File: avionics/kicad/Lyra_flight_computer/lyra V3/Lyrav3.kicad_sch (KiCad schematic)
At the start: 84 parts, among them J2 Screw_Terminal_01x06, J3 Conn_01x02, J4 Conn_01x02, J5 Conn_01x03, J6 Conn_01x06, J7 USB_B_Micro, J8 Conn_01x04, J9 Screw_Terminal_01x06, Q1 AO3401A, Q2 AO3400A, Q3 AO3400A, Q4 AO3400A, Q5 AO3400A, U1 AZ1117-3.3, U2 BMI088, U3 MPL3115A2, U4 ADXL375BCCZ-RL7, U5 LIS3MDL, U6 ADS1015IDGS, U7 W25Q64JVXGIQ, U8 RP2040, X1 S3D12.288000B20F30T

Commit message: real pretrip
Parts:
- removed C28: 100n, Capacitor_SMD:C_0603_1608Metric, symbol Device:C_Small
- removed R22: 1k, Resistor_SMD:R_0603_1608Metric, symbol Device:R_Small
- removed U7: W25Q64JVXGIQ, Package_SO:SOIC-8_5.23x5.23mm_P1.27mm, symbol easyeda2kicad:W25Q64JVXGIQ
- added C27: 100n, Capacitor_SMD:C_0603_1608Metric, symbol Device:C_Small
- added R14: 1k, Resistor_SMD:R_0603_1608Metric, symbol Device:R_Small
- added U9: W25Q128JVS, Package_SO:SOIC-8_5.23x5.23mm_P1.27mm, symbol Memory_Flash:W25Q128JVS
- J5: LCSC Part C160403 -> (none)
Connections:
- net +3V3: now also C27.1, U9.8 (VCC)
- net BOOTSEL: now also R14.2
- net GND: now also C27.2, U9.4 (GND)
- net QSPI_SCLK: now also U9.6 (CLK)
- net QSPI_SD1: now also U9.2 (DO(IO1))
- net QSPI_SD2: now also U9.3 (IO2)
- net QSPI_SD3: now also U9.7 (IO3)
- net QSPI_SDO: now also U9.5 (DI(IO0))
- net QSPI_SS: now also R14.1, U9.1 (~{CS})
- no-connect marks 30 -> 29

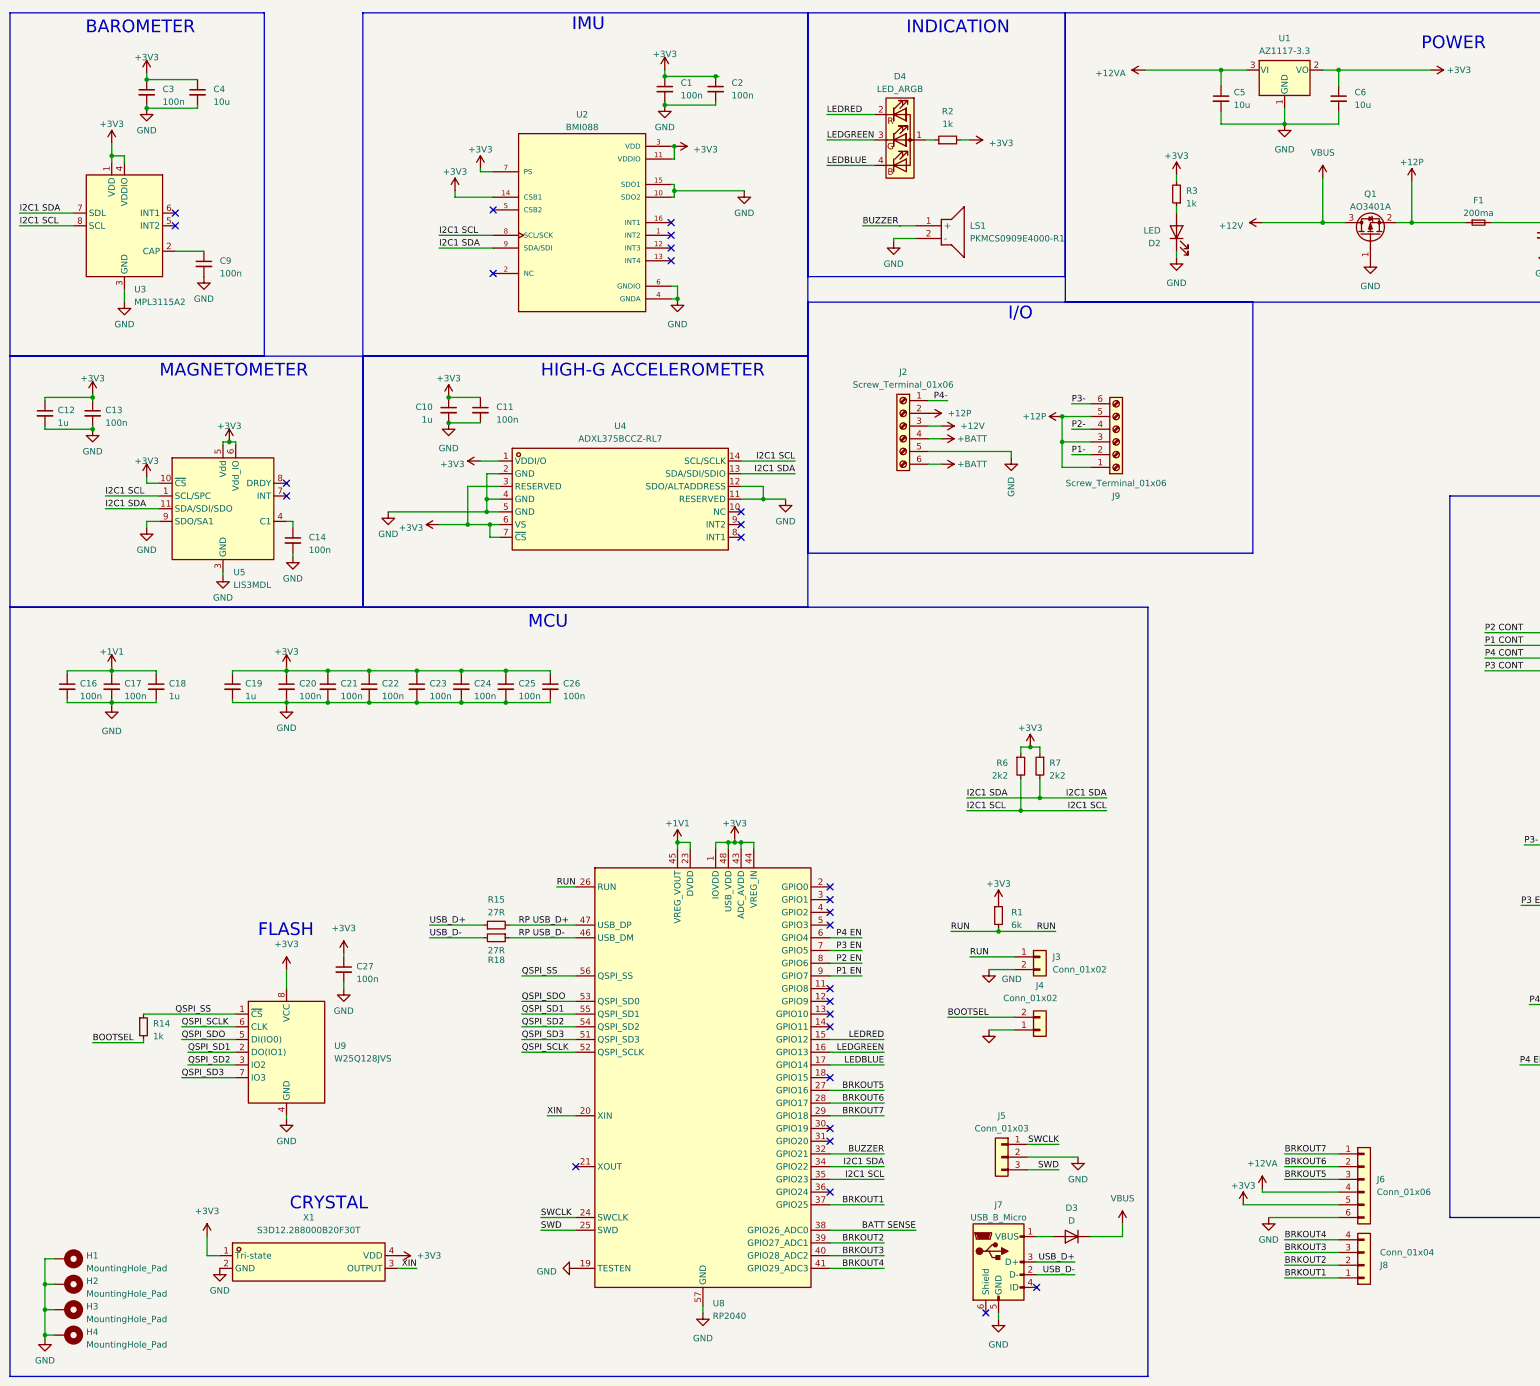
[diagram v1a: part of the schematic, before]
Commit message: change baro to dps310
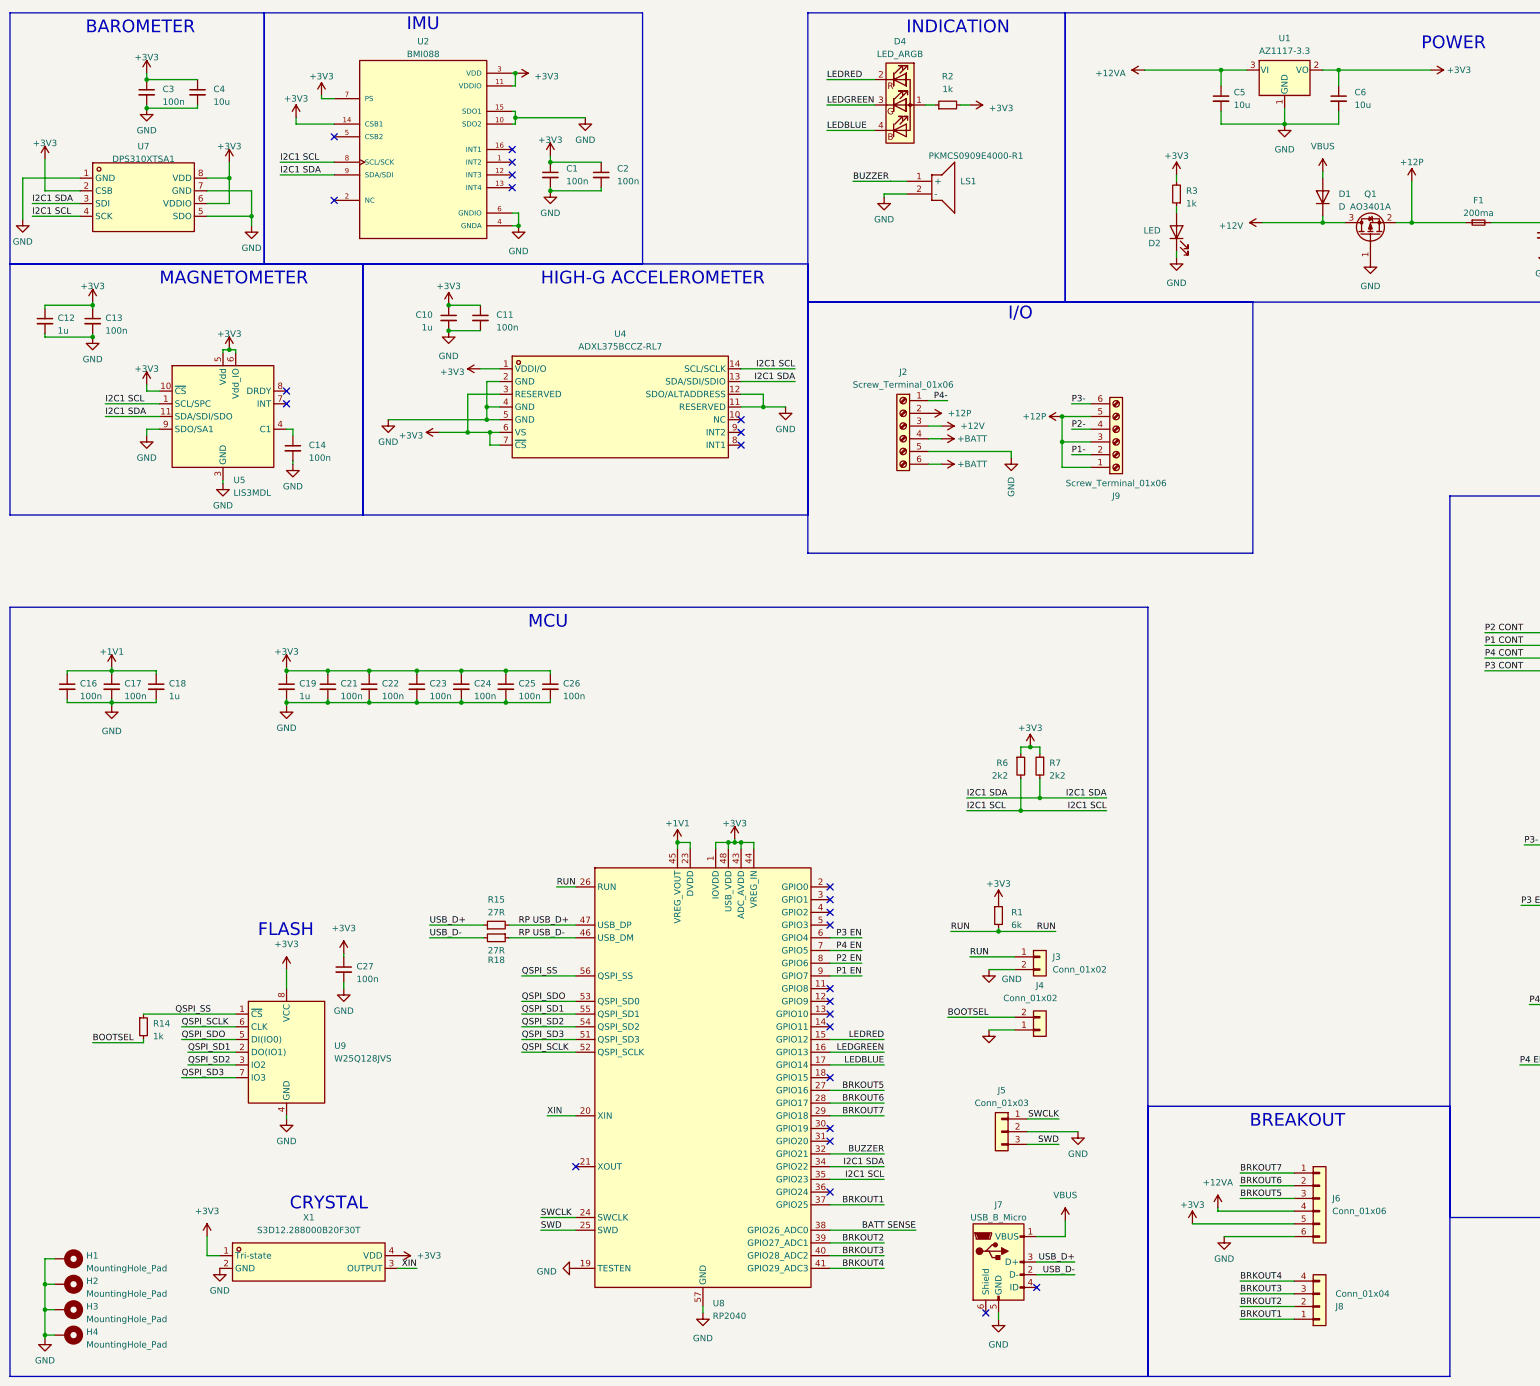
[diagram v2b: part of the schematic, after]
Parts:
- removed C20, C9: 100n, Capacitor_SMD:C_0603_1608Metric, symbol Device:C_Small
- removed D3: D, Diode_SMD:D_SOD-323, symbol Device:D
- removed U3: MPL3115A2, Package_LGA:NXP_LGA-8_3x5mm_P1.25mm_H1.1mm, symbol Sensor_Pressure:MPL3115A2
- added D1: D, Diode_SMD:D_SOD-323, symbol Device:D
- added U7: DPS310XTSA1, easyeda2kicad:LGA-8_DPS310XTSA1, symbol easyeda2kicad:DPS310XTSA1
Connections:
- net +12V: now also D1.1 (K)
- net +3V3: now also U7.2 (CSB), U7.6 (VDDIO), U7.8 (VDD)
- net GND: now also U7.1 (GND), U7.5 (SDO), U7.7 (GND)
- net I2C1 SCL: now also U7.4 (SCK)
- net I2C1 SDA: now also U7.3 (SDI)
- net P3 EN : now also U8.6 (GPIO4); no longer U8.7 (GPIO5)
- net P4 EN : now also U8.7 (GPIO5); no longer U8.6 (GPIO4)
- net VBUS: now reaches J7.1 (VBUS)
- net VBUS: now also D1.2 (A)
- no-connect marks 29 -> 27
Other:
- note added: "BREAKOUT"
- moved on the sheet: C1, C10, C11, C12, C13, C14, C19, C2, D4, J5, J6, J8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

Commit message: autosave before slep
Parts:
- added C9: 10u, Capacitor_SMD:C_0603_1608Metric, symbol Device:C_Small
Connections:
- net +12VA: now also C9.1, C9.2
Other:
- moved on the sheet: F1
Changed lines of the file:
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@@
   (junction (at 107.315 93.98) (diameter 0) (color 0 0 0 0)
   )
+  (junction (at 308.61 54.61) (diameter 0) (color 0 0 0 0)
+  )
   (junction (at 120.015 42.545) (diameter 0) (color 0 0 0 0)
   )
@@
     (stroke (width 0) (type default))
   )
+  (wire (pts (xy 308.61 54.61) (xy 318.77 54.61))
+    (stroke (width 0) (type default))
+  )
   (wire (pts (xy 175.895 258.445) (xy 186.69 258.445))
     (stroke (width 0) (type default))
@@
     (stroke (width 0) (type default))
   )
-  (wire (pts (xy 307.975 54.61) (xy 318.77 54.61))
+  (wire (pts (xy 302.895 54.61) (xy 308.61 54.61))
     (stroke (width 0) (type default))
   )
@@
     (stroke (width 0) (type default))
   )
-  (wire (pts (xy 292.1 54.61) (xy 302.895 54.61))
+  (wire (pts (xy 292.1 54.61) (xy 297.815 54.61))
     (stroke (width 0) (type default))
   )
@@
     )
   )
+  (symbol (lib_id "Device:C_Small") (at 308.61 52.07 0) (unit 1)
+    (in_bom yes) (on_board yes) (dnp no)
+    (property "Reference" "C9" (at 311.15 50.8 0)
+      (effects (font (size 1.27 1.27)) (justify left))
+    )
+    (property "Value" "10u" (at 311.15 53.34 0)
+      (effects (font (size 1.27 1.27)) (justify left))
+    )
+    (property "Footprint" "Capacitor_SMD:C_0603_1608Metric" (at 308.61 52.07 0)
+      (effects (font (size 1.27 1.27)) hide)
+    )
+    (property "Datasheet" "~" (at 308.61 52.07 0)
+      (effects (font (size 1.27 1.27)) hide)
+    )
+    (property "LCSC Part" "C19702" (at 308.61 52.07 0)
+      (effects (font (size 1.27 1.27)) hide)
+    )
+    (pin "1")
+    (pin "2")
+    (instances
+      (project "Lyrav3"
+        (path "/12cc3c39-e34e-4801-bd3f-38f875d59424"
+          (reference "C9") (unit 1)
+        )
+      )
+      (project "Board2"
+        (path "/3ee99ce6-1aa5-40d1-bb2e-7887993edb74"
+          (reference "C11") (unit 1)
+        )
+      )
+      (project "Lyra V2"
+        (path "/63622aab-8dfa-4523-a589-40aebeb23162"
+          (reference "C6") (unit 1)
+        )
+      )
+    )
+  )
   (symbol (lib_id "power:+3V3") (at 67.31 203.835 0) (unit 1)
     (in_bom yes) (on_board yes) (dnp no) (fields_autoplaced)
@@
     )
   )
+  (symbol (lib_id "power:+12VA") (at 308.61 49.53 0) (unit 1)
+    (in_bom yes) (on_board yes) (dnp no) (fields_autoplaced)
+    (property "Reference" "#PWR075" (at 308.61 53.34 0)
+      (effects (font (size 1.27 1.27)) hide)
+    )
+    (property "Value" "+12VA" (at 308.61 45.72 0)
+      (effects (font (size 1.27 1.27)))
+    )
+    (property "Footprint" "" (at 308.61 49.53 0)
+      (effects (font (size 1.27 1.27)) hide)
+    )
+    (property "Datasheet" "" (at 308.61 49.53 0)
+      (effects (font (size 1.27 1.27)) hide)
+    )
+    (pin "1")
+    (instances
+      (project "Lyrav3"
+        (path "/12cc3c39-e34e-4801-bd3f-38f875d59424"
+          (reference "#PWR075") (unit 1)
+        )
+      )
+      (project "Board2"
+        (path "/3ee99ce6-1aa5-40d1-bb2e-7887993edb74"
+          (reference "#PWR025") (unit 1)
+        )
+      )
+      (project "Lyra V2"
+        (path "/63622aab-8dfa-4523-a589-40aebeb23162"
+          (reference "#PWR08") (unit 1)
+        )
+      )
+    )
+  )
   (symbol (lib_id "power:GND") (at 352.044 191.643 0) (unit 1)
     (in_bom yes) (on_board yes) (dnp no) (fields_autoplaced)
@@
     )
   )
-  (symbol (lib_id "Device:Fuse_Small") (at 305.435 54.61 0) (unit 1)
+  (symbol (lib_id "Device:Fuse_Small") (at 300.355 54.61 0) (unit 1)
     (in_bom no) (on_board yes) (dnp no) (fields_autoplaced)
-    (property "Reference" "F1" (at 305.435 50.165 0)
+    (property "Reference" "F1" (at 300.355 50.165 0)
       (effects (font (size 1.27 1.27)))
     )
-    (property "Value" "200ma" (at 305.435 52.705 0)
+    (property "Value" "200ma" (at 300.355 52.705 0)
       (effects (font (size 1.27 1.27)))
     )
-    (property "Footprint" "Fuse:Fuse_0805_2012Metric" (at 305.435 54.61 0)
+    (property "Footprint" "Fuse:Fuse_0805_2012Metric" (at 300.355 54.61 0)
       (effects (font (size 1.27 1.27)) hide)
     )
-    (property "Datasheet" "~" (at 305.435 54.61 0)
+    (property "Datasheet" "~" (at 300.355 54.61 0)
       (effects (font (size 1.27 1.27)) hide)
     )
-    (property "LCSC_Part" "" (at 305.435 54.61 0)
+    (property "LCSC_Part" "" (at 300.355 54.61 0)
       (effects (font (size 1.27 1.27)) hide)
     )
-    (property "LCSC Part" "" (at 305.435 54.61 0)
+    (property "LCSC Part" "" (at 300.355 54.61 0)
       (effects (font (size 1.27 1.27)) hide)
     )

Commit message: buasuig
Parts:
- C9: value 10u -> 1000uf; footprint Capacitor_SMD:C_0603_1608Metric -> Capacitor_SMD:CP_Elec_6.3x3.9; now left out of the parts list
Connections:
- net +12VA: no longer C9.2
- net +3V3: now also U7.5 (SDO)
- net GND: now also C9.2; no longer U7.5 (SDO)
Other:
- moved on the sheet: C9
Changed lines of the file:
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@@
   (junction (at 333.629 178.943) (diameter 0) (color 0 0 0 0)
   )
+  (junction (at 305.435 54.61) (diameter 0) (color 0 0 0 0)
+  )
   (junction (at 400.05 185.42) (diameter 0) (color 0 0 0 0)
   )
@@
   (junction (at 366.395 221.615) (diameter 0) (color 0 0 0 0)
   )
-  (junction (at 60.325 53.34) (diameter 0) (color 0 0 0 0)
-  )
   (junction (at 333.629 199.898) (diameter 0) (color 0 0 0 0)
   )
   (junction (at 28.575 71.12) (diameter 0) (color 0 0 0 0)
   )
+  (junction (at 55.88 50.8) (diameter 0) (color 0 0 0 0)
+  )
   (junction (at 102.235 150.495) (diameter 0) (color 0 0 0 0)
   )
@@
   (junction (at 107.315 93.98) (diameter 0) (color 0 0 0 0)
   )
-  (junction (at 308.61 54.61) (diameter 0) (color 0 0 0 0)
-  )
   (junction (at 120.015 42.545) (diameter 0) (color 0 0 0 0)
   )
@@
     (stroke (width 0) (type default))
   )
+  (wire (pts (xy 55.88 50.8) (xy 55.88 53.34))
+    (stroke (width 0) (type default))
+  )
   (wire (pts (xy 111.76 197.485) (xy 125.095 197.485))
     (stroke (width 0) (type default))
@@
     (stroke (width 0) (type default))
   )
-  (wire (pts (xy 60.325 53.34) (xy 60.325 48.26))
+  (wire (pts (xy 305.435 60.325) (xy 305.435 59.69))
     (stroke (width 0) (type default))
   )
@@
     (stroke (width 0) (type default))
   )
+  (wire (pts (xy 55.88 53.34) (xy 51.435 53.34))
+    (stroke (width 0) (type default))
+  )
   (wire (pts (xy 93.345 263.525) (xy 89.535 263.525))
     (stroke (width 0) (type default))
@@
     (stroke (width 0) (type default))
   )
+  (wire (pts (xy 305.435 54.61) (xy 318.77 54.61))
+    (stroke (width 0) (type default))
+  )
   (wire (pts (xy 41.275 144.145) (xy 41.275 144.78))
     (stroke (width 0) (type default))
@@
     (stroke (width 0) (type default))
   )
-  (wire (pts (xy 308.61 54.61) (xy 318.77 54.61))
+  (wire (pts (xy 302.895 54.61) (xy 305.435 54.61))
     (stroke (width 0) (type default))
   )
@@
     (stroke (width 0) (type default))
   )
-  (wire (pts (xy 51.435 53.34) (xy 60.325 53.34))
-    (stroke (width 0) (type default))
-  )
   (wire (pts (xy 266.7 34.925) (xy 277.495 34.925))
     (stroke (width 0) (type default))
@@
     (stroke (width 0) (type default))
   )
-  (wire (pts (xy 302.895 54.61) (xy 308.61 54.61))
-    (stroke (width 0) (type default))
-  )
   (wire (pts (xy 182.245 202.565) (xy 175.895 202.565))
     (stroke (width 0) (type default))
@@
     (stroke (width 0) (type default))
   )
-  (wire (pts (xy 60.325 55.245) (xy 60.325 53.34))
+  (wire (pts (xy 60.325 48.26) (xy 60.325 55.245))
     (stroke (width 0) (type default))
   )
@@
     )
   )
-  (symbol (lib_id "Device:C_Small") (at 308.61 52.07 0) (unit 1)
-    (in_bom yes) (on_board yes) (dnp no)
-    (property "Reference" "C9" (at 311.15 50.8 0)
+  (symbol (lib_id "Device:C_Small") (at 305.435 57.15 0) (unit 1)
+    (in_bom no) (on_board yes) (dnp no)
+    (property "Reference" "C9" (at 307.975 55.88 0)
       (effects (font (size 1.27 1.27)) (justify left))
     )
-    (property "Value" "10u" (at 311.15 53.34 0)
+    (property "Value" "1000uf" (at 307.975 58.42 0)
       (effects (font (size 1.27 1.27)) (justify left))
     )
-    (property "Footprint" "Capacitor_SMD:C_0603_1608Metric" (at 308.61 52.07 0)
+    (property "Footprint" "Capacitor_SMD:CP_Elec_6.3x3.9" (at 305.435 57.15 0)
       (effects (font (size 1.27 1.27)) hide)
     )
-    (property "Datasheet" "~" (at 308.61 52.07 0)
+    (property "Datasheet" "~" (at 305.435 57.15 0)
       (effects (font (size 1.27 1.27)) hide)
     )
-    (property "LCSC Part" "C19702" (at 308.61 52.07 0)
+    (property "LCSC Part" "C19702" (at 305.435 57.15 0)
       (effects (font (size 1.27 1.27)) hide)
     )
@@
     )
   )
-  (symbol (lib_id "power:+12VA") (at 308.61 49.53 0) (unit 1)
-    (in_bom yes) (on_board yes) (dnp no) (fields_autoplaced)
-    (property "Reference" "#PWR075" (at 308.61 53.34 0)
-      (effects (font (size 1.27 1.27)) hide)
-    )
-    (property "Value" "+12VA" (at 308.61 45.72 0)
-      (effects (font (size 1.27 1.27)))
-    )
-    (property "Footprint" "" (at 308.61 49.53 0)
-      (effects (font (size 1.27 1.27)) hide)
-    )
-    (property "Datasheet" "" (at 308.61 49.53 0)
-      (effects (font (size 1.27 1.27)) hide)
-    )
-    (pin "1")
-    (instances
-      (project "Lyrav3"
-        (path "/12cc3c39-e34e-4801-bd3f-38f875d59424"
-          (reference "#PWR075") (unit 1)
-        )
-      )
-      (project "Board2"
-        (path "/3ee99ce6-1aa5-40d1-bb2e-7887993edb74"
-          (reference "#PWR025") (unit 1)
-        )
-      )
-      (project "Lyra V2"
-        (path "/63622aab-8dfa-4523-a589-40aebeb23162"
-          (reference "#PWR08") (unit 1)
-        )
-      )
-    )
-  )
   (symbol (lib_id "power:GND") (at 352.044 191.643 0) (unit 1)
     (in_bom yes) (on_board yes) (dnp no) (fields_autoplaced)
@@
         )
       )
+    )
+  )
+  (symbol (lib_id "power:GND") (at 305.435 60.325 0) (unit 1)
+    (in_bom yes) (on_board yes) (dnp no) (fields_autoplaced)
+    (property "Reference" "#PWR075" (at 305.435 66.675 0)
+      (effects (font (size 1.27 1.27)) hide)
+    )
+    (property "Value" "GND" (at 305.435 64.77 0)
+      (effects (font (size 1.27 1.27)))
+    )
+    (property "Footprint" "" (at 305.435 60.325 0)
+      (effects (font (size 1.27 1.27)) hide)
+    )
+    (property "Datasheet" "" (at 305.435 60.325 0)
+      (effects (font (size 1.27 1.27)) hide)
+    )
+    (pin "1")
+    (instances
+      (project "Lyrav3"
+        (path "/12cc3c39-e34e-4801-bd3f-38f875d59424"
+          (reference "#PWR075") (unit 1)
+        )
+      )

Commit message: found new brownout cap
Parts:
- C9: footprint Capacitor_SMD:CP_Elec_6.3x3.9 -> Capacitor_THT:CP_Radial_D8.0mm_P3.80mm
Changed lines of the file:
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@@
       (effects (font (size 1.27 1.27)) (justify left))
     )
-    (property "Footprint" "Capacitor_SMD:CP_Elec_6.3x3.9" (at 305.435 57.15 0)
+    (property "Footprint" "Capacitor_THT:CP_Radial_D8.0mm_P3.80mm" (at 305.435 57.15 0)
       (effects (font (size 1.27 1.27)) hide)
     )
